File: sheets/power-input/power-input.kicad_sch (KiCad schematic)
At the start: 7 parts, among them J1 Eurorack Power

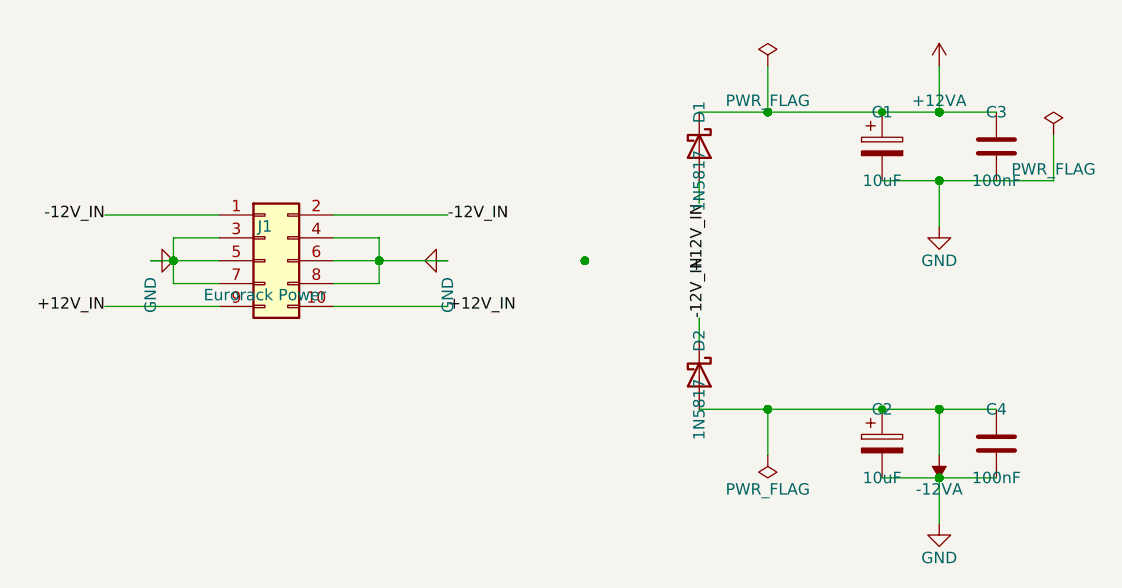
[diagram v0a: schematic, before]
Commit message: Use the shared 1N5817 symbol
D1 and D2 now use Eurorack Common:1N5817 instead of the stock Diode library, so the footprint and 3D model come pre-linked. Submodule pin moves to the commit that adds the symbol.

Includes the layout fixes made in Eeschema. ERC reports 0 violations.
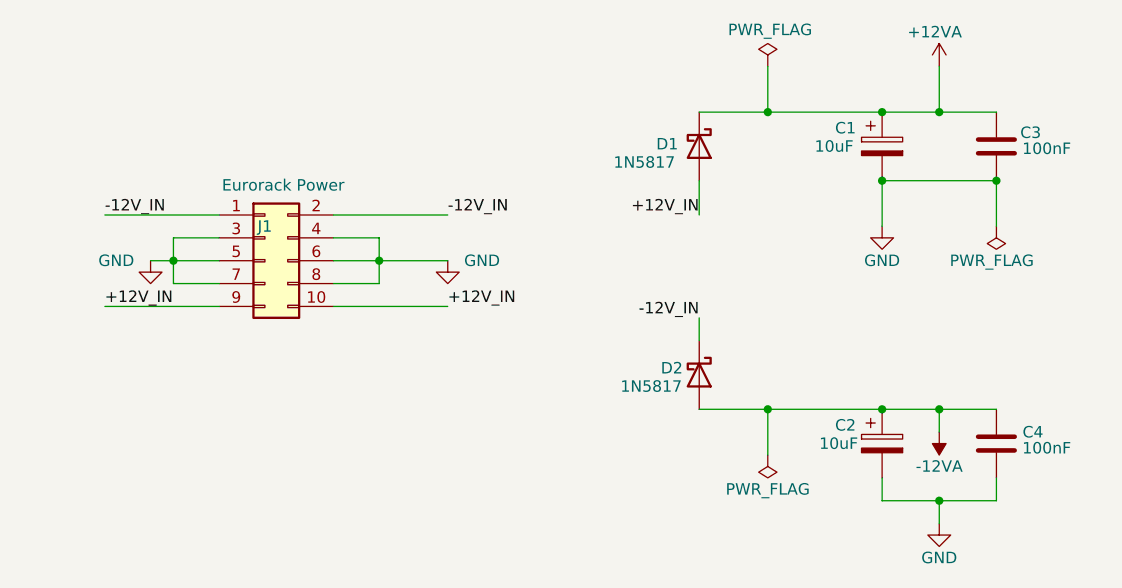
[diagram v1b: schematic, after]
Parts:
- D1, D2: symbol Diode:1N5817 -> Eurorack Common:1N5817

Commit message: Document the power input block and set the docs convention
Remove C3 and C4. HF decoupling belongs at each IC power pin, in the block that holds the IC, not at the connector. Trim the rails and reconnect the GND PWR_FLAG. ERC reports 0 violations.

Each block now carries a README in Simplified Technical English. The Limits section records what a reader cannot see from the schematic: the headroom the series diodes cost, the missing fuse and rail filter, and the diode direction that ERC cannot check.
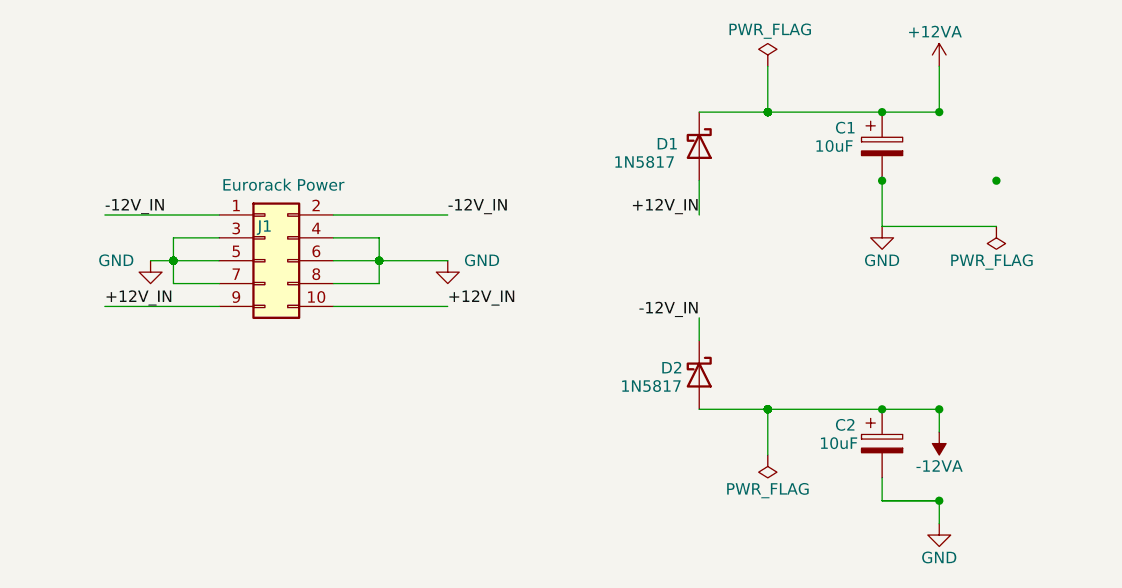
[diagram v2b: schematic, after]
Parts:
- removed C3, C4: 100nF, symbol Eurorack Common:C_100nF_50V_X7R_2.5mm

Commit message: Restore rail PWR_FLAG connections after layout tidy
The layout tidy is a clear improvement: no overlapping text, labels clear of the symbol, and one GND spine joining both capacitors.

The two rails lost their PWR_FLAG connection, so ERC reported them as not driven. PWR_FLAG only satisfies ERC on the net it sits on, and a diode is passive, so a flag on +12V_IN does not drive +12VA. Added a flag on each rail.

ERC reports 0 violations.
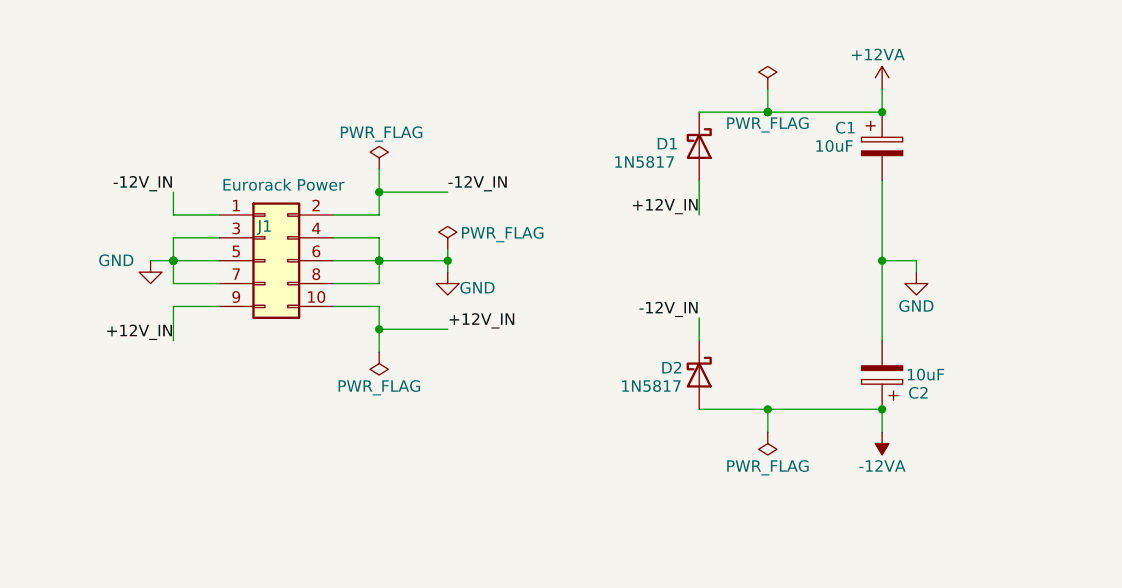
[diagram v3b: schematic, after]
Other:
- moved on the sheet: C2

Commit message: Keep one PWR_FLAG per driven net
Remove the flags on +12V_IN and -12V_IN. A flag only satisfies ERC on its own net, and a passive diode does not carry driven status to the rail, so those two did nothing. One flag each on +12VA, -12VA and GND is the minimum correct set.

ERC reports 0 violations with power_pin_not_driven still set to error.
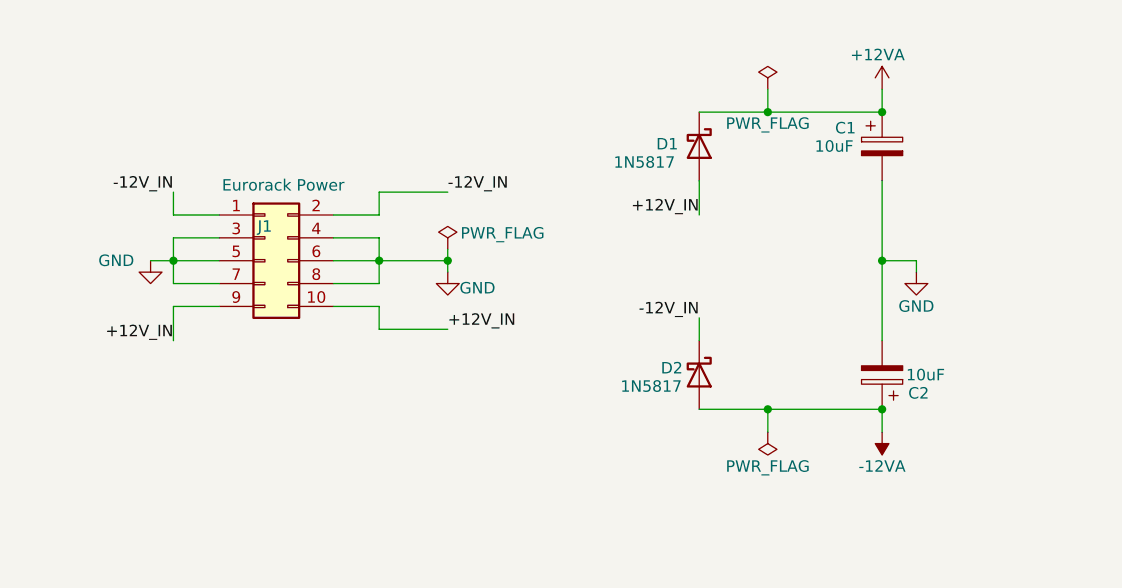
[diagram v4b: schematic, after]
